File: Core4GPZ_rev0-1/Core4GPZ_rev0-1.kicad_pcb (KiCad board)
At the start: 2 copper layers, 78.7 x 105.2 mm, 47 parts, among them IC1 MAX9926UAEE_V+, M3 MountingHole_3.2mm_M3_DIN965_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, Q1 FGD3440G2-F085, Q2 FGD3440G2-F085, U2 core4, U3 MPXHZ6250AC6T1, U5 LMV321

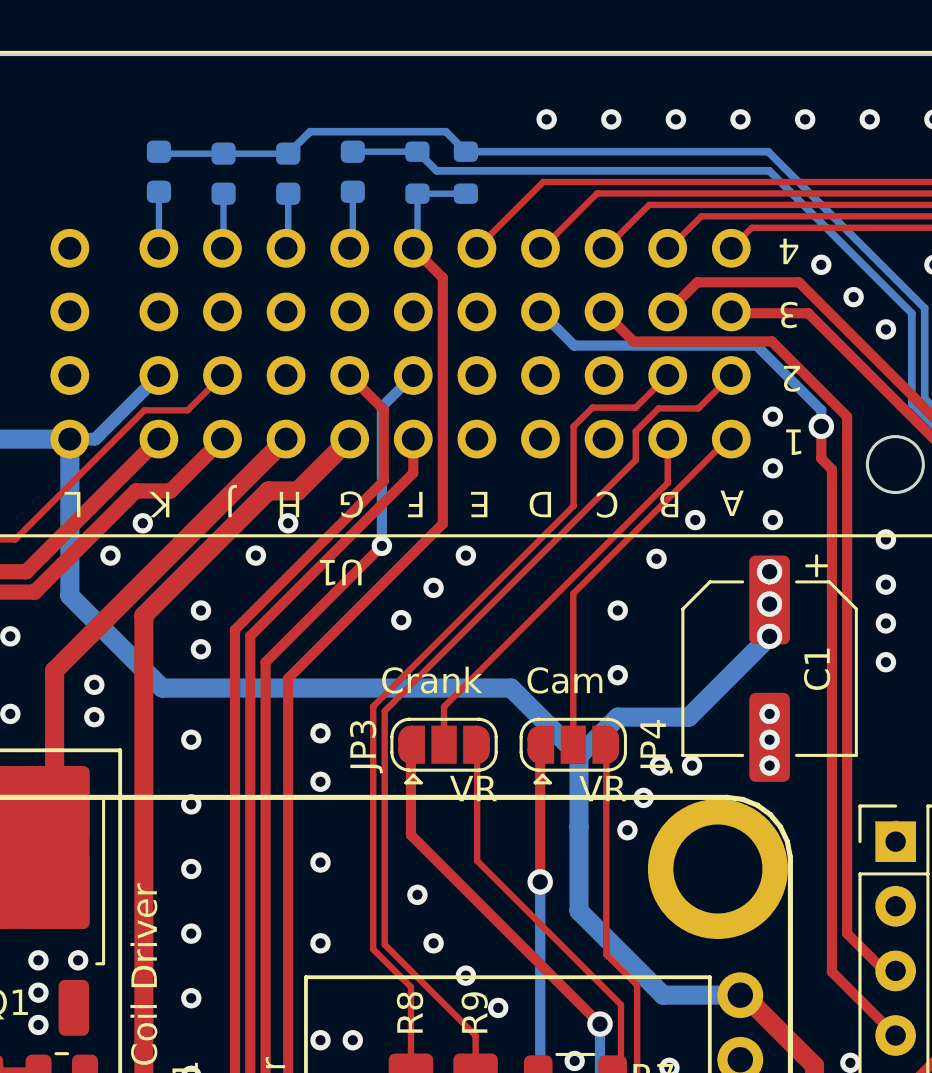
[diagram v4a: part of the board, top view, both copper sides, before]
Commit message: Removed NeutralSwitch. Added Up-Shifter support
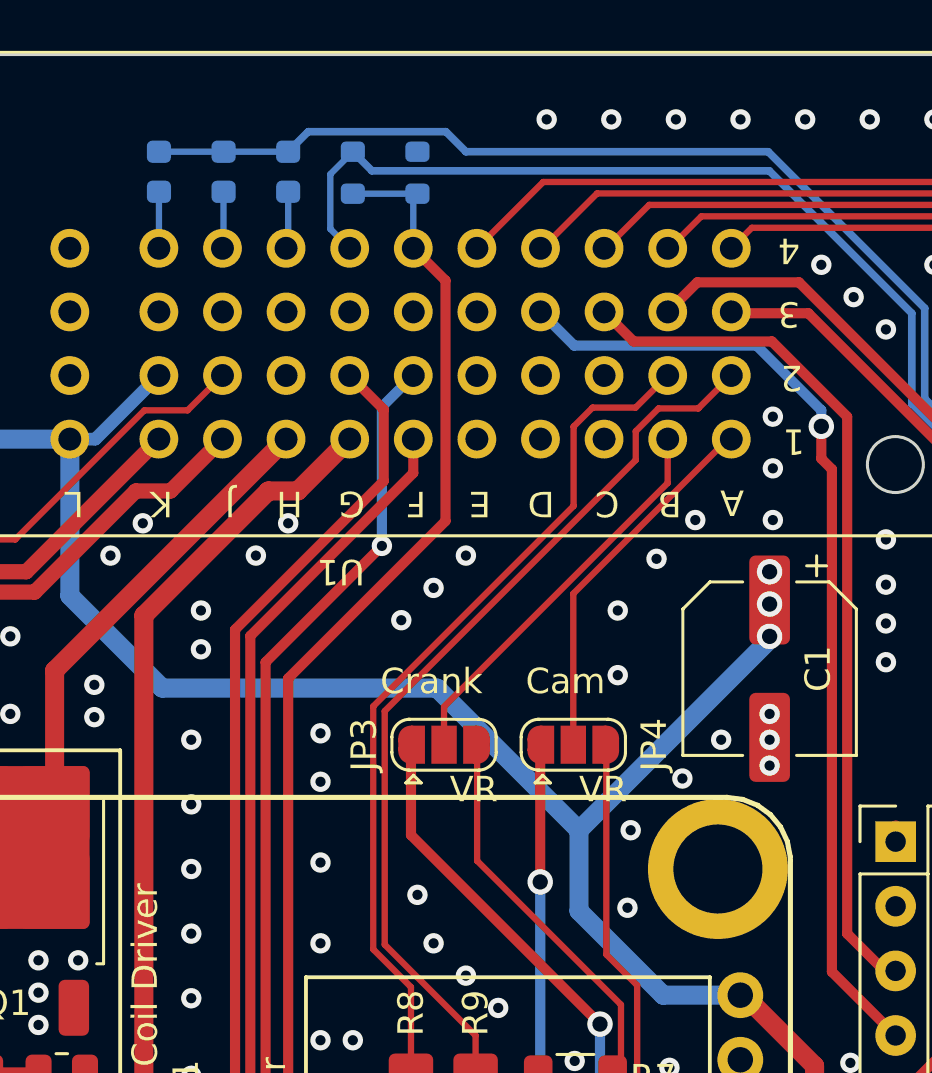
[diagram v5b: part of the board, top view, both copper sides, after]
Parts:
- removed D4: D, Diode_SMD:D_0603_1608Metric
- moved R2 2.54 mm to (116.8, 43.4)
- moved R1 1.91 mm to (119.4, 43.4)
- moved D2 0.07 mm to (111.8, 43.3)
- moved D3 0.07 mm to (114.3, 43.3)
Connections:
- net Clutch_SWITCH renamed Clutch_SW
- net SPR1_SWITCH renamed NEUTRAL_SW
- net SideStand_SWITCH renamed SideStand_SW
- R2 pad 2: NEUTRAL_SIGNAL -> SHIFT+
- U1 pad 37: Neutral_SWITCH -> SHIFT+
- U2 pad 100: GND -> (no net)
- U2 pad 101: GND -> (no net)
- U2 pad 102: GND -> (no net)
- U2 pad 103: GND -> (no net)
- U2 pad 17: /NEUTRAL_LIGHT -> unconnected-(U2A-D36-Pad17)
- U2 pad 44: NEUTRAL_SIGNAL -> SHIFT+
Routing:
- net SHIFT+: track 0.00 -> 111.6 mm
- net NEUTRAL_SIGNAL: track 106.6 -> 0.00 mm
- net Neutral_SWITCH: track 2.63 -> 0.00 mm
- net SNSR_+5V: track 145.5 -> 146.4 mm

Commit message: Reorganised Schematic
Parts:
- removed C4: 1uF, Capacitor_SMD:C_0805_2012Metric_Pad1.18x1.45mm_HandSolder
- removed D7: D_Schottky, Diode_SMD:D_PowerDI-123
- removed U5: LMV321, Package_TO_SOT_SMD:SOT-23-5_HandSoldering
- added C2: 100nF, Capacitor_SMD:C_0805_2012Metric_Pad1.18x1.45mm_HandSolder, F.Cu at (138.2, 93.8)
- added D4: D_Schottky, Diode_SMD:D_PowerDI-123, F.Cu at (135.1, 86.5)
- added U4: LMV321, Package_TO_SOT_SMD:SOT-23-5_HandSoldering, F.Cu at (121.9, 111.8)
- C3: value 100nF -> 1uF
- moved JP6 0.52 mm to (123.2, 108.1)
- moved JP5 0.40 mm to (125.9, 107.4)
- moved C3 0.26 mm to (135.9, 93.8)
- moved C1 0.09 mm to (133.2, 62.8)
- moved A1 0.06 mm to (138.2, 69.7)
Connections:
- net /CLT_5V renamed CLT_5V
- net /CLT_SNSR renamed CLT_SNSR
- net /DIR renamed DIR
- net /EN renamed EN
- net /STEP renamed STEP
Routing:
- net CLT_5V: track 8.99 -> 9.55 mm
- net GND: vias 255 -> 258

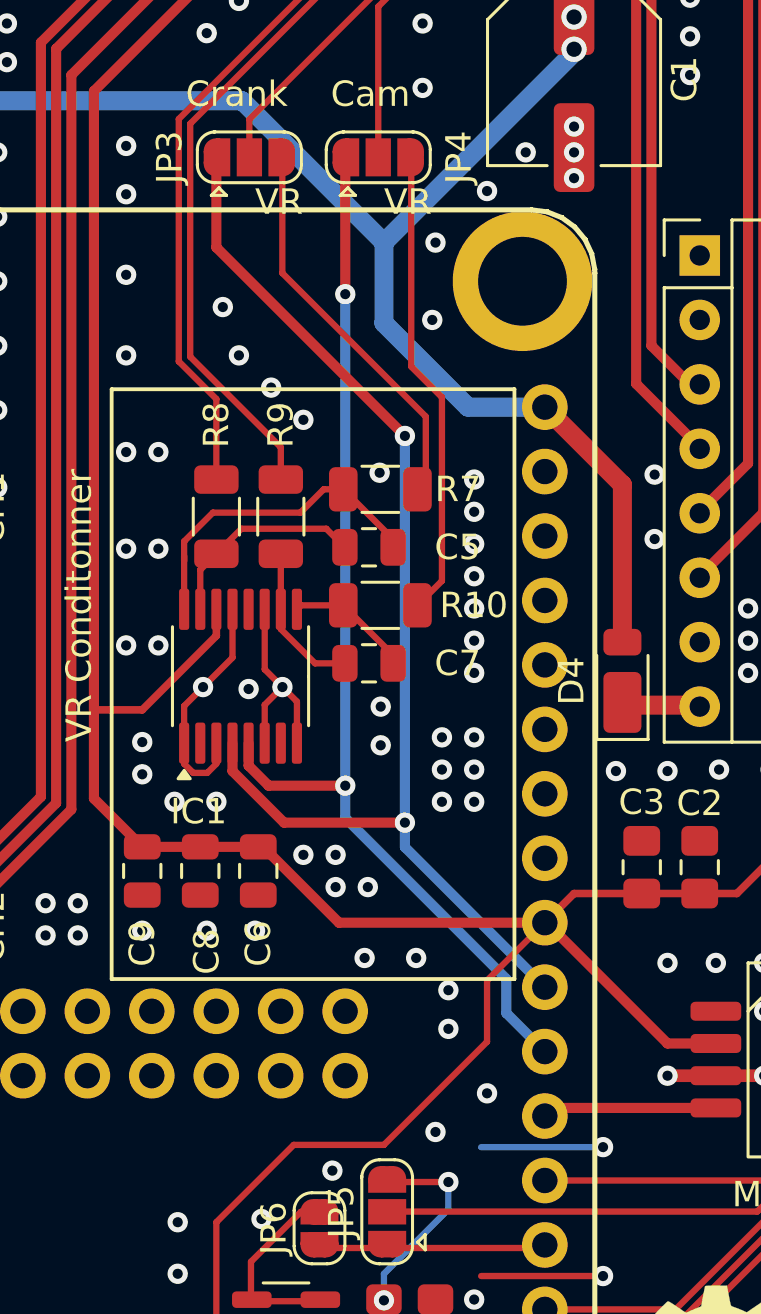
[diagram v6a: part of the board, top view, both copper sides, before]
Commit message: Added pullup resistor on VR Conditionner
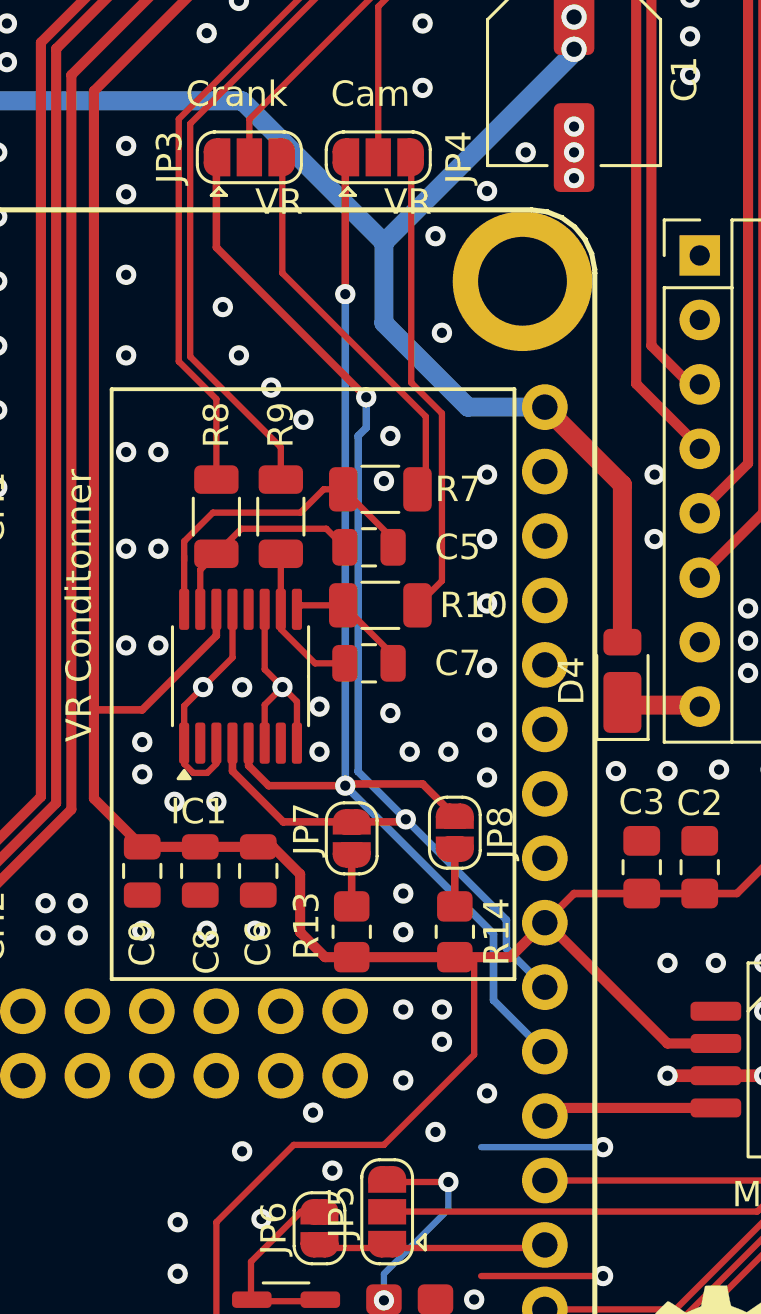
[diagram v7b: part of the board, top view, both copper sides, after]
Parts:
- added JP7: Crank Pull-Up, Jumper:SolderJumper-2_P1.3mm_Open_RoundedPad1.0x1.5mm, F.Cu at (124.5, 92.7)
- added JP8: Cam Pull-up, Jumper:SolderJumper-2_P1.3mm_Open_RoundedPad1.0x1.5mm, F.Cu at (128.5, 92.5)
- added R13: 1k, Resistor_SMD:R_0805_2012Metric_Pad1.20x1.40mm_HandSolder, F.Cu at (124.5, 96.4)
- added R14: 1k, Resistor_SMD:R_0805_2012Metric_Pad1.20x1.40mm_HandSolder, F.Cu at (128.5, 96.4)
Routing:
- net CAM_SIGNAL: track 43.5 -> 48.4 mm
- net Net-(JP8-B): track 0.00 -> 2.26 mm
- net Net-(JP7-B): track 0.00 -> 2.03 mm
- net GND: vias 258 -> 255

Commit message: Added Gerber files
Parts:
- moved JP1 0.25 mm to (94.7, 78.6)
- moved Q2 0.12 mm to (103.6, 87.0)
- moved U1 0.09 mm to (116.8, 41.2)
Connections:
- U2 pad 100: (no net) -> GND
- U2 pad 101: (no net) -> GND
- U2 pad 102: (no net) -> GND
- U2 pad 103: (no net) -> GND
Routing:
- net GND: track 75.7 -> 75.2 mm, vias 255 -> 265
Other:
- board text added: "OUT"
- board text added: "© Gabriel Wulveryck CERN-OHL-S-2.0 license Based on the Speeduino Project https://github.com/G-Maveryck"
- board text removed: "© Gabriel Wulveryck CERN-OHL-S-2.0 license Based on the Speeduino Project Doc : github.com/G-Maveryck"
